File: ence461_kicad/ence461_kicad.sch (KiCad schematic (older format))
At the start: 98 parts, among them J1 SWD, J2 INPUT_0, J3 INPUT_1, J4 CANBUS, J5 INPUT_2, J6 POWER, Q1 Q_PMOS_GSD, U1 LMV324, U2 LMV324, U3 LMV324, U4 74HC3G14DP, U5 LMV321, U6 NCV7344D13R2GOSCT-ND, U7 MIC5202, U9 MKE16Z32VLD4

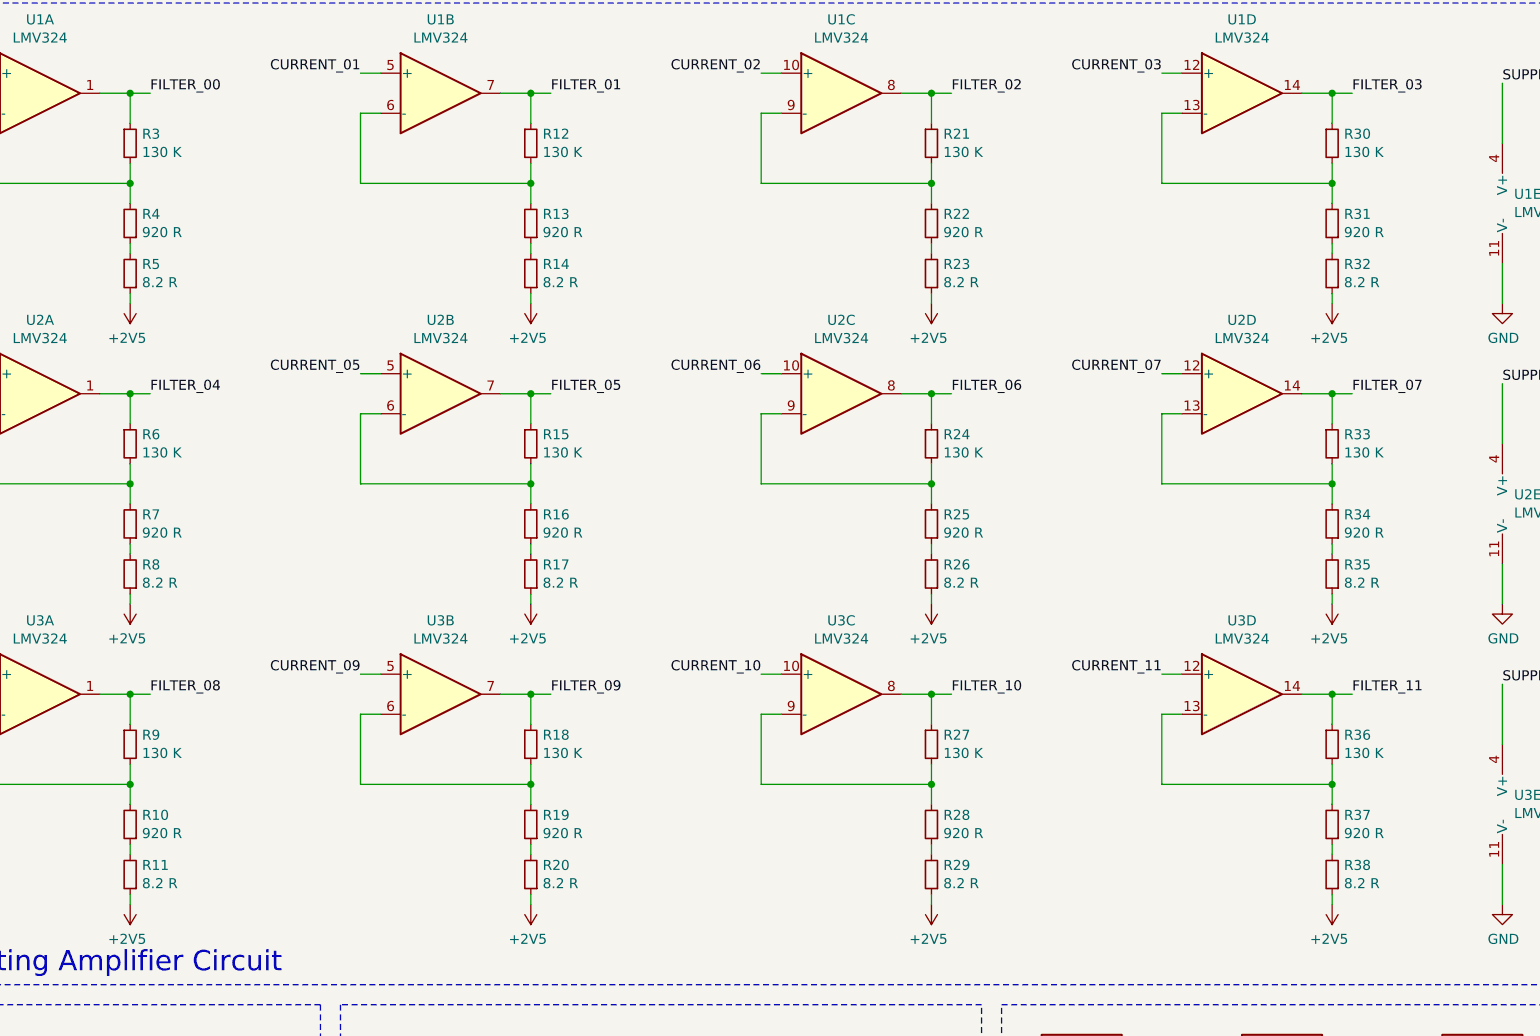
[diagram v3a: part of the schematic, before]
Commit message: Changed gain stage to equal 100
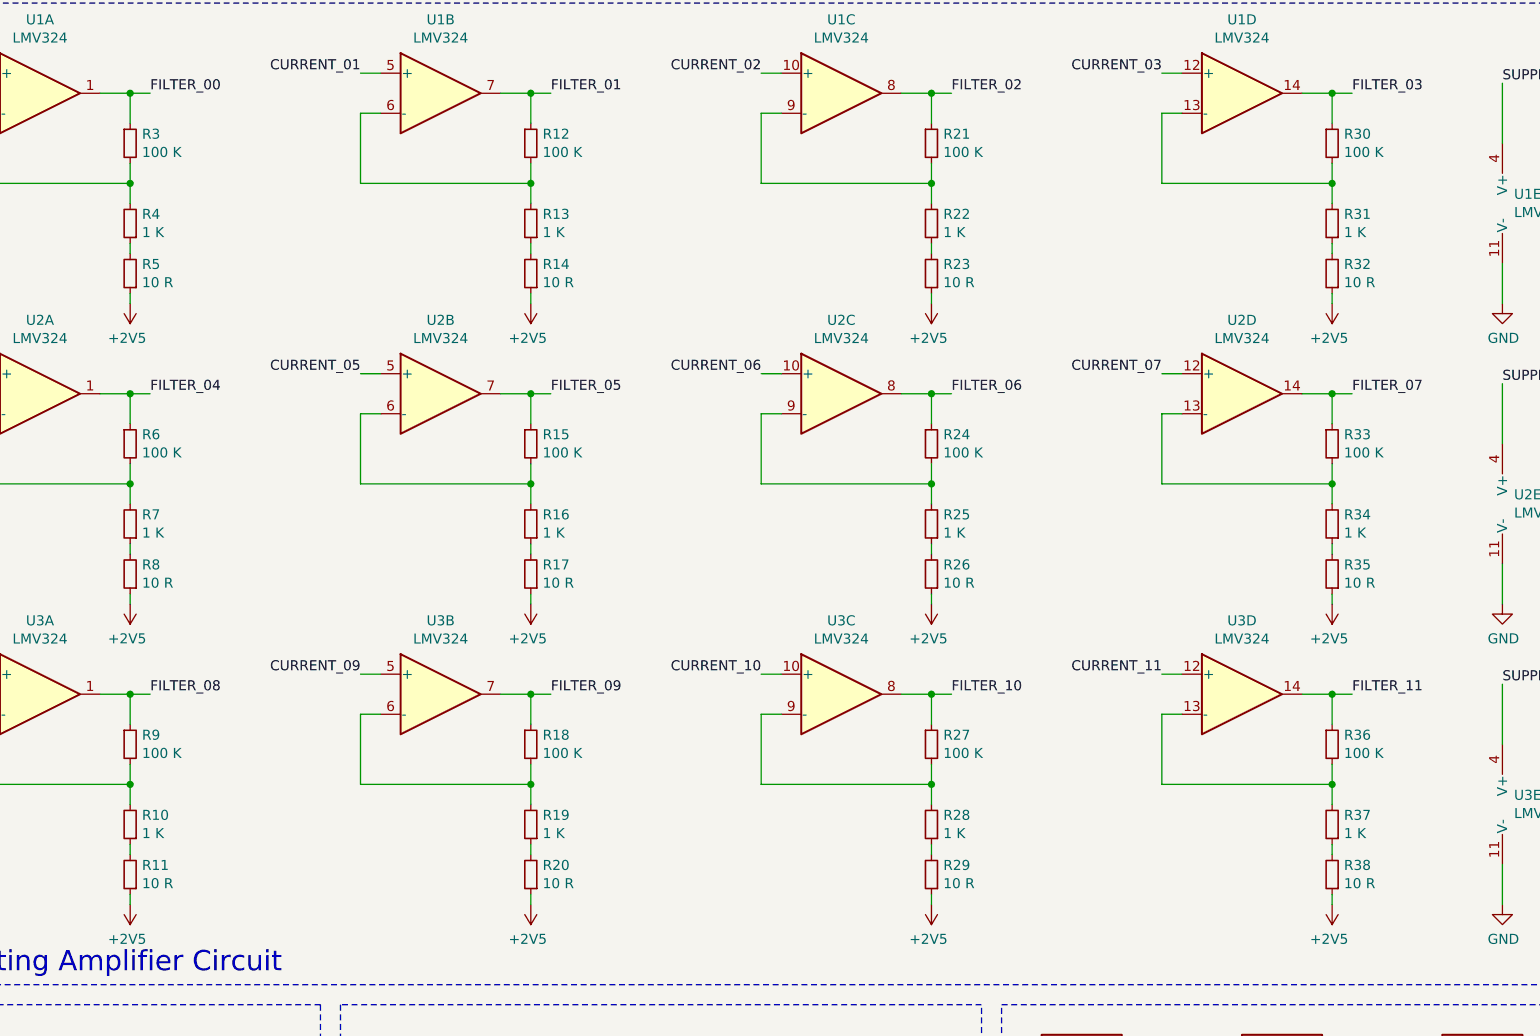
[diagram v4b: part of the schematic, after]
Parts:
- R10, R13, R16, R19, R22, R25, R28, R31, R34, R37, R4, R7: value 920 R -> 1 K
- R11, R14, R17, R20, R23, R26, R29, R32, R35, R38, R5, R8: value 8.2 R -> 10 R
- R12, R15, R18, R21, R24, R27, R3, R30, R33, R36, R6, R9: value 130 K -> 100 K
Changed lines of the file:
@@
 P 2150 1250
 F 0 "R3" H 2209 1296 50  0000 L CNN
-F 1 "130 K" H 2209 1205 50  0000 L CNN
+F 1 "100 K" H 2209 1205 50  0000 L CNN
 F 2 "Resistor_SMD:R_0603_1608Metric" H 2150 1250 50  0001 C CNN
 F 3 "~" H 2150 1250 50  0001 C CNN
@@
 P 2150 1650
 F 0 "R4" H 2091 1604 50  0000 R CNN
-F 1 "920 R" H 2091 1695 50  0000 R CNN
+F 1 "1 K" H 2091 1695 50  0000 R CNN
 F 2 "Resistor_SMD:R_0603_1608Metric" H 2150 1650 50  0001 C CNN
 F 3 "~" H 2150 1650 50  0001 C CNN
@@
 P 4150 1250
 F 0 "R12" H 4209 1296 50  0000 L CNN
-F 1 "130 K" H 4209 1205 50  0000 L CNN
+F 1 "100 K" H 4209 1205 50  0000 L CNN
 F 2 "Resistor_SMD:R_0603_1608Metric" H 4150 1250 50  0001 C CNN
 F 3 "~" H 4150 1250 50  0001 C CNN
@@
 P 4150 1650
 F 0 "R13" H 4091 1604 50  0000 R CNN
-F 1 "920 R" H 4091 1695 50  0000 R CNN
+F 1 "1 K" H 4091 1695 50  0000 R CNN
 F 2 "Resistor_SMD:R_0603_1608Metric" H 4150 1650 50  0001 C CNN
 F 3 "~" H 4150 1650 50  0001 C CNN
@@
 P 6150 1250
 F 0 "R21" H 6209 1296 50  0000 L CNN
-F 1 "130 K" H 6209 1205 50  0000 L CNN
+F 1 "100 K" H 6209 1205 50  0000 L CNN
 F 2 "Resistor_SMD:R_0603_1608Metric" H 6150 1250 50  0001 C CNN
 F 3 "~" H 6150 1250 50  0001 C CNN
@@
 P 6150 1650
 F 0 "R22" H 6091 1604 50  0000 R CNN
-F 1 "920 R" H 6091 1695 50  0000 R CNN
+F 1 "1 K" H 6091 1695 50  0000 R CNN
 F 2 "Resistor_SMD:R_0603_1608Metric" H 6150 1650 50  0001 C CNN
 F 3 "~" H 6150 1650 50  0001 C CNN
@@
 P 8150 1250
 F 0 "R30" H 8209 1296 50  0000 L CNN
-F 1 "130 K" H 8209 1205 50  0000 L CNN
+F 1 "100 K" H 8209 1205 50  0000 L CNN
 F 2 "Resistor_SMD:R_0603_1608Metric" H 8150 1250 50  0001 C CNN
 F 3 "~" H 8150 1250 50  0001 C CNN
@@
 P 8150 1650
 F 0 "R31" H 8091 1604 50  0000 R CNN
-F 1 "920 R" H 8091 1695 50  0000 R CNN
+F 1 "1 K" H 8091 1695 50  0000 R CNN
 F 2 "Resistor_SMD:R_0603_1608Metric" H 8150 1650 50  0001 C CNN
 F 3 "~" H 8150 1650 50  0001 C CNN
@@
 P 2150 1900
 F 0 "R5" H 2091 1854 50  0000 R CNN
-F 1 "8.2 R" H 2091 1945 50  0000 R CNN
+F 1 "10 R" H 2091 1945 50  0000 R CNN
 F 2 "Resistor_SMD:R_0603_1608Metric" H 2150 1900 50  0001 C CNN
 F 3 "~" H 2150 1900 50  0001 C CNN
@@
 P 4150 1900
 F 0 "R14" H 4091 1854 50  0000 R CNN
-F 1 "8.2 R" H 4091 1945 50  0000 R CNN
+F 1 "10 R" H 4091 1945 50  0000 R CNN
 F 2 "Resistor_SMD:R_0603_1608Metric" H 4150 1900 50  0001 C CNN
 F 3 "~" H 4150 1900 50  0001 C CNN
@@
 P 6150 1900
 F 0 "R23" H 6091 1854 50  0000 R CNN
-F 1 "8.2 R" H 6091 1945 50  0000 R CNN
+F 1 "10 R" H 6091 1945 50  0000 R CNN
 F 2 "Resistor_SMD:R_0603_1608Metric" H 6150 1900 50  0001 C CNN
 F 3 "~" H 6150 1900 50  0001 C CNN
@@
 P 8150 1900
 F 0 "R32" H 8091 1854 50  0000 R CNN
-F 1 "8.2 R" H 8091 1945 50  0000 R CNN
+F 1 "10 R" H 8091 1945 50  0000 R CNN
 F 2 "Resistor_SMD:R_0603_1608Metric" H 8150 1900 50  0001 C CNN
 F 3 "~" H 8150 1900 50  0001 C CNN
@@
 P 2150 2750
 F 0 "R6" H 2209 2796 50  0000 L CNN
-F 1 "130 K" H 2209 2705 50  0000 L CNN
+F 1 "100 K" H 2209 2705 50  0000 L CNN
 F 2 "Resistor_SMD:R_0603_1608Metric" H 2150 2750 50  0001 C CNN
 F 3 "~" H 2150 2750 50  0001 C CNN
@@
 P 2150 3150
 F 0 "R7" H 2091 3104 50  0000 R CNN
-F 1 "920 R" H 2091 3195 50  0000 R CNN
+F 1 "1 K" H 2091 3195 50  0000 R CNN
 F 2 "Resistor_SMD:R_0603_1608Metric" H 2150 3150 50  0001 C CNN
 F 3 "~" H 2150 3150 50  0001 C CNN
@@
 P 4150 2750
 F 0 "R15" H 4209 2796 50  0000 L CNN
-F 1 "130 K" H 4209 2705 50  0000 L CNN
+F 1 "100 K" H 4209 2705 50  0000 L CNN
 F 2 "Resistor_SMD:R_0603_1608Metric" H 4150 2750 50  0001 C CNN
 F 3 "~" H 4150 2750 50  0001 C CNN
@@
 P 4150 3150
 F 0 "R16" H 4091 3104 50  0000 R CNN
-F 1 "920 R" H 4091 3195 50  0000 R CNN
+F 1 "1 K" H 4091 3195 50  0000 R CNN
 F 2 "Resistor_SMD:R_0603_1608Metric" H 4150 3150 50  0001 C CNN
 F 3 "~" H 4150 3150 50  0001 C CNN
@@
 P 6150 2750
 F 0 "R24" H 6209 2796 50  0000 L CNN
-F 1 "130 K" H 6209 2705 50  0000 L CNN
+F 1 "100 K" H 6209 2705 50  0000 L CNN
 F 2 "Resistor_SMD:R_0603_1608Metric" H 6150 2750 50  0001 C CNN
 F 3 "~" H 6150 2750 50  0001 C CNN
@@
 P 6150 3150
 F 0 "R25" H 6091 3104 50  0000 R CNN
-F 1 "920 R" H 6091 3195 50  0000 R CNN
+F 1 "1 K" H 6091 3195 50  0000 R CNN
 F 2 "Resistor_SMD:R_0603_1608Metric" H 6150 3150 50  0001 C CNN
 F 3 "~" H 6150 3150 50  0001 C CNN
@@
 P 8150 2750
 F 0 "R33" H 8209 2796 50  0000 L CNN
-F 1 "130 K" H 8209 2705 50  0000 L CNN
+F 1 "100 K" H 8209 2705 50  0000 L CNN
 F 2 "Resistor_SMD:R_0603_1608Metric" H 8150 2750 50  0001 C CNN
 F 3 "~" H 8150 2750 50  0001 C CNN
@@
 P 8150 3150
 F 0 "R34" H 8091 3104 50  0000 R CNN
-F 1 "920 R" H 8091 3195 50  0000 R CNN
+F 1 "1 K" H 8091 3195 50  0000 R CNN
 F 2 "Resistor_SMD:R_0603_1608Metric" H 8150 3150 50  0001 C CNN
 F 3 "~" H 8150 3150 50  0001 C CNN
@@
 P 2150 3400
 F 0 "R8" H 2091 3354 50  0000 R CNN
-F 1 "8.2 R" H 2091 3445 50  0000 R CNN
+F 1 "10 R" H 2091 3445 50  0000 R CNN
 F 2 "Resistor_SMD:R_0603_1608Metric" H 2150 3400 50  0001 C CNN
 F 3 "~" H 2150 3400 50  0001 C CNN
@@
 P 4150 3400
 F 0 "R17" H 4091 3354 50  0000 R CNN
-F 1 "8.2 R" H 4091 3445 50  0000 R CNN
+F 1 "10 R" H 4091 3445 50  0000 R CNN
 F 2 "Resistor_SMD:R_0603_1608Metric" H 4150 3400 50  0001 C CNN
 F 3 "~" H 4150 3400 50  0001 C CNN
@@
 P 6150 3400
 F 0 "R26" H 6091 3354 50  0000 R CNN
-F 1 "8.2 R" H 6091 3445 50  0000 R CNN
+F 1 "10 R" H 6091 3445 50  0000 R CNN
 F 2 "Resistor_SMD:R_0603_1608Metric" H 6150 3400 50  0001 C CNN
 F 3 "~" H 6150 3400 50  0001 C CNN
@@
 P 8150 3400
 F 0 "R35" H 8091 3354 50  0000 R CNN
-F 1 "8.2 R" H 8091 3445 50  0000 R CNN
+F 1 "10 R" H 8091 3445 50  0000 R CNN
 F 2 "Resistor_SMD:R_0603_1608Metric" H 8150 3400 50  0001 C CNN
 F 3 "~" H 8150 3400 50  0001 C CNN
@@
 P 2150 4250
 F 0 "R9" H 2209 4296 50  0000 L CNN
-F 1 "130 K" H 2209 4205 50  0000 L CNN
+F 1 "100 K" H 2209 4205 50  0000 L CNN
 F 2 "Resistor_SMD:R_0603_1608Metric" H 2150 4250 50  0001 C CNN
 F 3 "~" H 2150 4250 50  0001 C CNN
@@
 P 2150 4650
 F 0 "R10" H 2091 4604 50  0000 R CNN
-F 1 "920 R" H 2091 4695 50  0000 R CNN
+F 1 "1 K" H 2091 4695 50  0000 R CNN
 F 2 "Resistor_SMD:R_0603_1608Metric" H 2150 4650 50  0001 C CNN
 F 3 "~" H 2150 4650 50  0001 C CNN
@@
 P 4150 4250
 F 0 "R18" H 4209 4296 50  0000 L CNN
-F 1 "130 K" H 4209 4205 50  0000 L CNN
+F 1 "100 K" H 4209 4205 50  0000 L CNN
 F 2 "Resistor_SMD:R_0603_1608Metric" H 4150 4250 50  0001 C CNN
 F 3 "~" H 4150 4250 50  0001 C CNN
@@
 P 4150 4650
 F 0 "R19" H 4091 4604 50  0000 R CNN
-F 1 "920 R" H 4091 4695 50  0000 R CNN
+F 1 "1 K" H 4091 4695 50  0000 R CNN
 F 2 "Resistor_SMD:R_0603_1608Metric" H 4150 4650 50  0001 C CNN
 F 3 "~" H 4150 4650 50  0001 C CNN
@@
 P 6150 4250
 F 0 "R27" H 6209 4296 50  0000 L CNN
-F 1 "130 K" H 6209 4205 50  0000 L CNN
+F 1 "100 K" H 6209 4205 50  0000 L CNN
 F 2 "Resistor_SMD:R_0603_1608Metric" H 6150 4250 50  0001 C CNN
 F 3 "~" H 6150 4250 50  0001 C CNN
@@
 P 6150 4650
 F 0 "R28" H 6091 4604 50  0000 R CNN
-F 1 "920 R" H 6091 4695 50  0000 R CNN
+F 1 "1 K" H 6091 4695 50  0000 R CNN
 F 2 "Resistor_SMD:R_0603_1608Metric" H 6150 4650 50  0001 C CNN
 F 3 "~" H 6150 4650 50  0001 C CNN
@@
 P 8150 4250
 F 0 "R36" H 8209 4296 50  0000 L CNN
-F 1 "130 K" H 8209 4205 50  0000 L CNN
+F 1 "100 K" H 8209 4205 50  0000 L CNN
 F 2 "Resistor_SMD:R_0603_1608Metric" H 8150 4250 50  0001 C CNN
 F 3 "~" H 8150 4250 50  0001 C CNN
@@
 P 8150 4650
 F 0 "R37" H 8091 4604 50  0000 R CNN
-F 1 "920 R" H 8091 4695 50  0000 R CNN
+F 1 "1 K" H 8091 4695 50  0000 R CNN
 F 2 "Resistor_SMD:R_0603_1608Metric" H 8150 4650 50  0001 C CNN
 F 3 "~" H 8150 4650 50  0001 C CNN
@@
 P 2150 4900
 F 0 "R11" H 2091 4854 50  0000 R CNN
-F 1 "8.2 R" H 2091 4945 50  0000 R CNN
+F 1 "10 R" H 2091 4945 50  0000 R CNN
 F 2 "Resistor_SMD:R_0603_1608Metric" H 2150 4900 50  0001 C CNN
 F 3 "~" H 2150 4900 50  0001 C CNN
@@
 P 4150 4900
 F 0 "R20" H 4091 4854 50  0000 R CNN
-F 1 "8.2 R" H 4091 4945 50  0000 R CNN
+F 1 "10 R" H 4091 4945 50  0000 R CNN
 F 2 "Resistor_SMD:R_0603_1608Metric" H 4150 4900 50  0001 C CNN
 F 3 "~" H 4150 4900 50  0001 C CNN
@@
 P 6150 4900
 F 0 "R29" H 6091 4854 50  0000 R CNN
-F 1 "8.2 R" H 6091 4945 50  0000 R CNN
+F 1 "10 R" H 6091 4945 50  0000 R CNN
 F 2 "Resistor_SMD:R_0603_1608Metric" H 6150 4900 50  0001 C CNN
 F 3 "~" H 6150 4900 50  0001 C CNN
@@
 P 8150 4900
 F 0 "R38" H 8091 4854 50  0000 R CNN
-F 1 "8.2 R" H 8091 4945 50  0000 R CNN
+F 1 "10 R" H 8091 4945 50  0000 R CNN
 F 2 "Resistor_SMD:R_0603_1608Metric" H 8150 4900 50  0001 C CNN
 F 3 "~" H 8150 4900 50  0001 C CNN

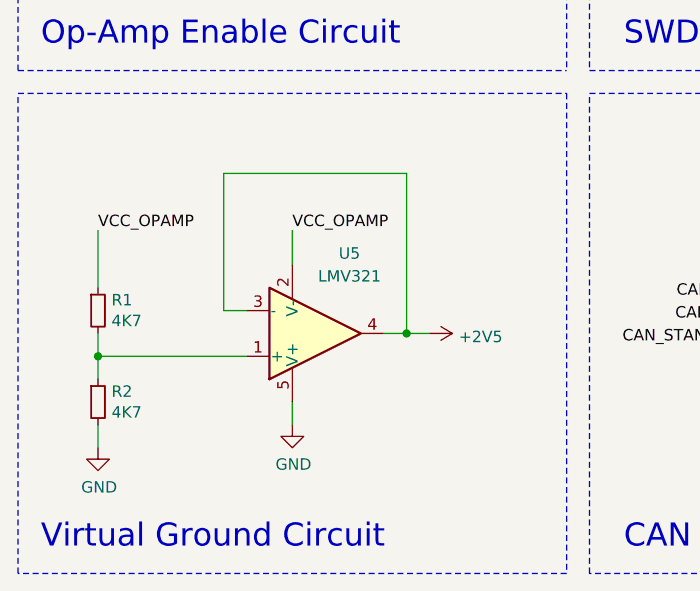
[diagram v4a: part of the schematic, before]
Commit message: Added schematics for diagrams. Fixed virtual ground mistake.
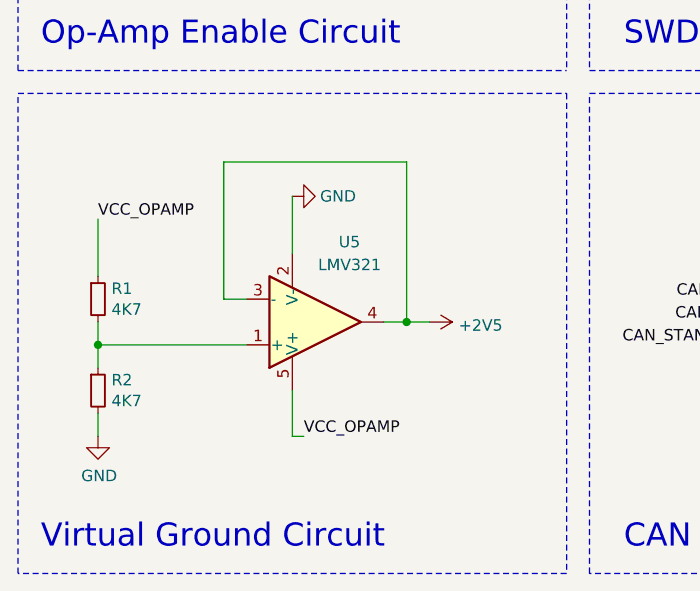
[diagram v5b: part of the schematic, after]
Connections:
- net GND: now also U5.2 (V-); no longer U5.5 (V+)
- net VCC_OPAMP: now also U5.5 (V+); no longer U5.2 (V-)
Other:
- moved on the sheet: R1, R2, U5
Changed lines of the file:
@@
 L Amplifier_Operational:LMV321 U5
 U 1 1 5ED02868
-P 2000 10100
-F 0 "U5" H 2150 9750 50  0000 C CNN
-F 1 "LMV321" H 2150 9850 50  0000 C CNN
-F 2 "Package_TO_SOT_SMD:SOT-23-5" H 2000 10100 50  0001 L CNN
-F 3 "http://www.ti.com/lit/ds/symlink/lmv324.pdf" H 2000 10100 50  0001 C CNN
-	1    2000 10100
+P 2000 10050
+F 0 "U5" H 2150 9700 50  0000 C CNN
+F 1 "LMV321" H 2150 9800 50  0000 C CNN
+F 2 "Package_TO_SOT_SMD:SOT-23-5" H 2000 10050 50  0001 L CNN
+F 3 "http://www.ti.com/lit/ds/symlink/lmv324.pdf" H 2000 10050 50  0001 C CNN
+	1    2000 10050
 	1    0    0    1
 $EndComp
@@
 L Device:R_Small R1
 U 1 1 5ED034A0
-P 1050 10000
-F 0 "R1" H 1109 10046 50  0000 L CNN
-F 1 "4K7" H 1109 9955 50  0000 L CNN
-F 2 "Resistor_SMD:R_0603_1608Metric" H 1050 10000 50  0001 C CNN
-F 3 "~" H 1050 10000 50  0001 C CNN
-	1    1050 10000
+P 1050 9950
+F 0 "R1" H 1109 9996 50  0000 L CNN
+F 1 "4K7" H 1109 9905 50  0000 L CNN
+F 2 "Resistor_SMD:R_0603_1608Metric" H 1050 9950 50  0001 C CNN
+F 3 "~" H 1050 9950 50  0001 C CNN
+	1    1050 9950
 	1    0    0    -1
 $EndComp
@@
 L Device:R_Small R2
 U 1 1 5ED03AD8
-P 1050 10400
-F 0 "R2" H 1109 10446 50  0000 L CNN
-F 1 "4K7" H 1109 10355 50  0000 L CNN
-F 2 "Resistor_SMD:R_0603_1608Metric" H 1050 10400 50  0001 C CNN
-F 3 "~" H 1050 10400 50  0001 C CNN
-	1    1050 10400
+P 1050 10350
+F 0 "R2" H 1109 10396 50  0000 L CNN
+F 1 "4K7" H 1109 10305 50  0000 L CNN
+F 2 "Resistor_SMD:R_0603_1608Metric" H 1050 10350 50  0001 C CNN
+F 3 "~" H 1050 10350 50  0001 C CNN
+	1    1050 10350
 	1    0    0    -1
 $EndComp
@@
 L power:GND #PWR06
 U 1 1 5ED05553
-P 1900 10500
-F 0 "#PWR06" H 1900 10250 50  0001 C CNN
-F 1 "GND" H 1905 10327 50  0000 C CNN
-F 2 "" H 1900 10500 50  0001 C CNN
-F 3 "" H 1900 10500 50  0001 C CNN
-	1    1900 10500
-	1    0    0    -1
+P 1900 9500
+F 0 "#PWR06" H 1900 9250 50  0001 C CNN
+F 1 "GND" V 1900 9300 50  0000 C CNN
+F 2 "" H 1900 9500 50  0001 C CNN
+F 3 "" H 1900 9500 50  0001 C CNN
+	1    1900 9500
+	0    -1   -1   0
 $EndComp
 $Comp
 L power:+2V5 #PWR010
 U 1 1 5ED057B1
-P 2500 10100
-F 0 "#PWR010" H 2500 9950 50  0001 C CNN
-F 1 "+2V5" V 2515 10228 50  0000 L CNN
-F 2 "" H 2500 10100 50  0001 C CNN
-F 3 "" H 2500 10100 50  0001 C CNN
-	1    2500 10100
+P 2500 10050
+F 0 "#PWR010" H 2500 9900 50  0001 C CNN
+F 1 "+2V5" V 2515 10178 50  0000 L CNN
+F 2 "" H 2500 10050 50  0001 C CNN
+F 3 "" H 2500 10050 50  0001 C CNN
+	1    2500 10050
 	0    1    1    0
 $EndComp
 Wire Wire Line
-	1700 10000 1600 10000
-Wire Wire Line
-	1600 10000 1600 9400
-Wire Wire Line
-	1600 9400 2400 9400
-Wire Wire Line
-	2400 9400 2400 10100
-Wire Wire Line
-	2400 10100 2300 10100
-Wire Wire Line
-	2400 10100 2500 10100
-Connection ~ 2400 10100
-Wire Wire Line
-	1900 10400 1900 10500
-Wire Wire Line
-	1700 10200 1050 10200
-Wire Wire Line
-	1050 10200 1050 10300
-Wire Wire Line
-	1050 10200 1050 10100
-Connection ~ 1050 10200
+	1700 9950 1600 9950
+Wire Wire Line
+	1600 9950 1600 9350
+Wire Wire Line
+	1600 9350 2400 9350
+Wire Wire Line
+	2400 9350 2400 10050
+Wire Wire Line
+	2400 10050 2300 10050
+Wire Wire Line
+	2400 10050 2500 10050
+Connection ~ 2400 10050
+Wire Wire Line
+	1700 10150 1050 10150
+Wire Wire Line
+	1050 10150 1050 10250
+Wire Wire Line
+	1050 10150 1050 10050
+Connection ~ 1050 10150
 $Comp
 L power:GND #PWR02
 U 1 1 5ED10590
-P 1050 10600
-F 0 "#PWR02" H 1050 10350 50  0001 C CNN
-F 1 "GND" H 1055 10427 50  0000 C CNN
-F 2 "" H 1050 10600 50  0001 C CNN
-F 3 "" H 1050 10600 50  0001 C CNN
-	1    1050 10600
-	1    0    0    -1
-$EndComp
-Wire Wire Line
-	1050 10500 1050 10600
+P 1050 10550
+F 0 "#PWR02" H 1050 10300 50  0001 C CNN
+F 1 "GND" H 1055 10377 50  0000 C CNN
+F 2 "" H 1050 10550 50  0001 C CNN
+F 3 "" H 1050 10550 50  0001 C CNN
+	1    1050 10550
+	1    0    0    -1
+$EndComp
+Wire Wire Line
+	1050 10450 1050 10550
 $Comp
 L Amplifier_Operational:LMV324 U2
@@
 Text Label 4450 9550 2    50   ~ 0
 VCC_MICRO
-Text Label 1900 9650 0    50   ~ 0
+Text Label 1950 10550 0    50   ~ 0
 VCC_OPAMP
-Wire Wire Line
-	1900 9650 1900 9800
-Text Label 1050 9650 0    50   ~ 0
+Text Label 1050 9600 0    50   ~ 0
 VCC_OPAMP
 Wire Wire Line
-	1050 9650 1050 9900
+	1050 9600 1050 9850
 Text Label 1800 7450 0    50   ~ 0
 VCC_OPAMP
@@
 Text Notes 9950 8850 0    101  ~ 0
 Microcontroller
+Wire Wire Line
+	1900 9500 1900 9750
+Wire Wire Line
+	1950 10550 1900 10550
+Wire Wire Line
+	1900 10350 1900 10550
 $EndSCHEMATC
